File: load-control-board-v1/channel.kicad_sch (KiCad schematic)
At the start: 30 parts, among them Q2 IRFP7530PBF, U10 OPA188xxDBV, U11 INA186A1IDCKR, U9 OPA188xxDBV

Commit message: lc2kicad
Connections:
- net I_sink_mon_0 renamed I_sink_mon
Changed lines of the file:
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@@
 	)
 	(label "V_Rs0n"
-		(at 208.28 54.61 0)
+		(at 168.91 68.58 0)
 		(effects
 			(font
@@
 	)
 	(label "V_Rs0n"
-		(at 168.91 68.58 0)
+		(at 208.28 54.61 0)
 		(effects
 			(font
@@
 			)
 			(justify left bottom)
-		)
-	)
-	(global_label "I_sink_mon_0"
-		(shape input)
-		(at 248.92 69.85 0)
-		(fields_autoplaced yes)
-		(effects
-			(font
-				(size 1.27 1.27)
-			)
-			(justify left)
-		)
-		(property "Intersheetrefs" "${INTERSHEET_REFS}"
-			(at 264.4236 69.85 0)
-			(effects
-				(font
-					(size 1.27 1.27)
-				)
-				(justify left)
-				(hide yes)
-			)
 		)
 	)
@@
 		)
 	)
+	(hierarchical_label "I_sink_mon"
+		(shape input)
+		(at 248.92 69.85 0)
+		(effects
+			(font
+				(size 1.27 1.27)
+			)
+			(justify left)
+		)
+	)

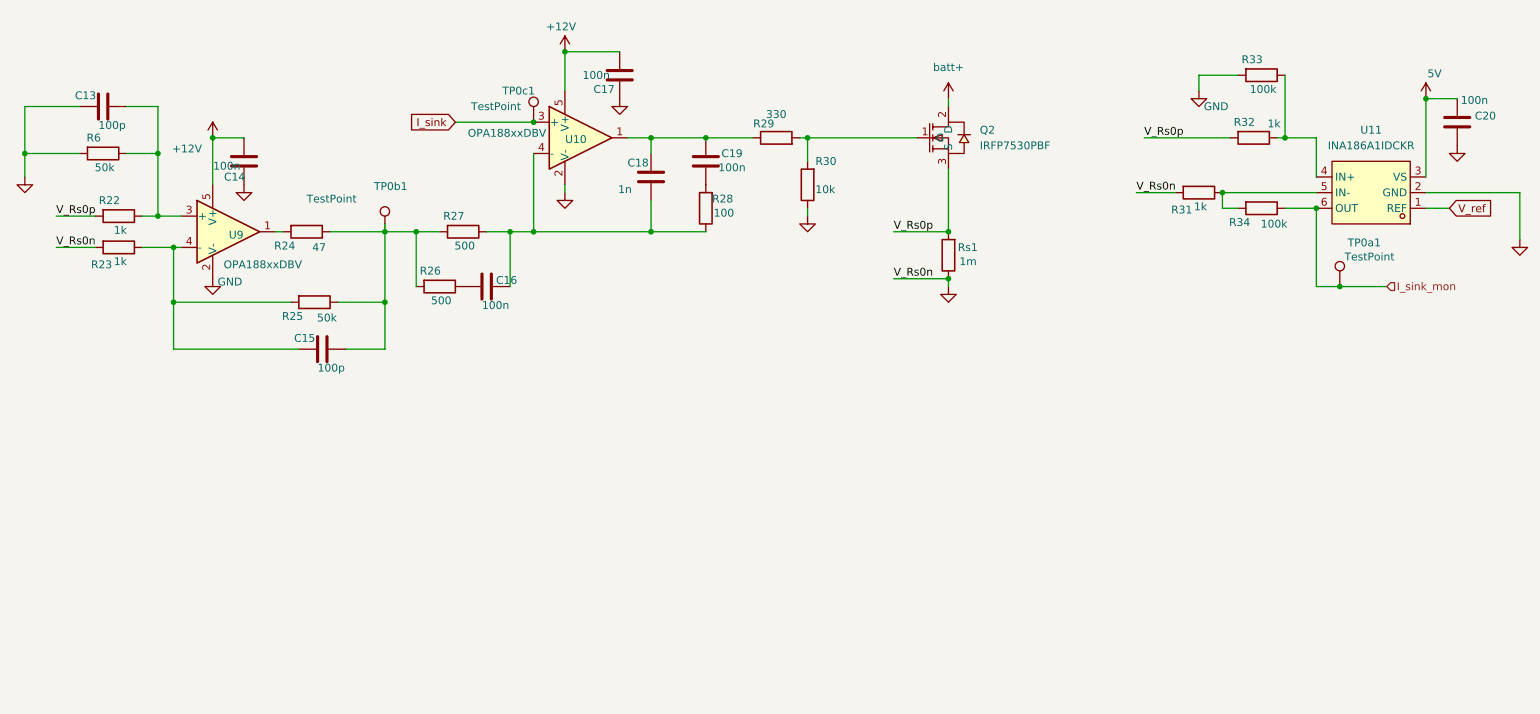
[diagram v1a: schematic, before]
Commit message: Edit multi opamp
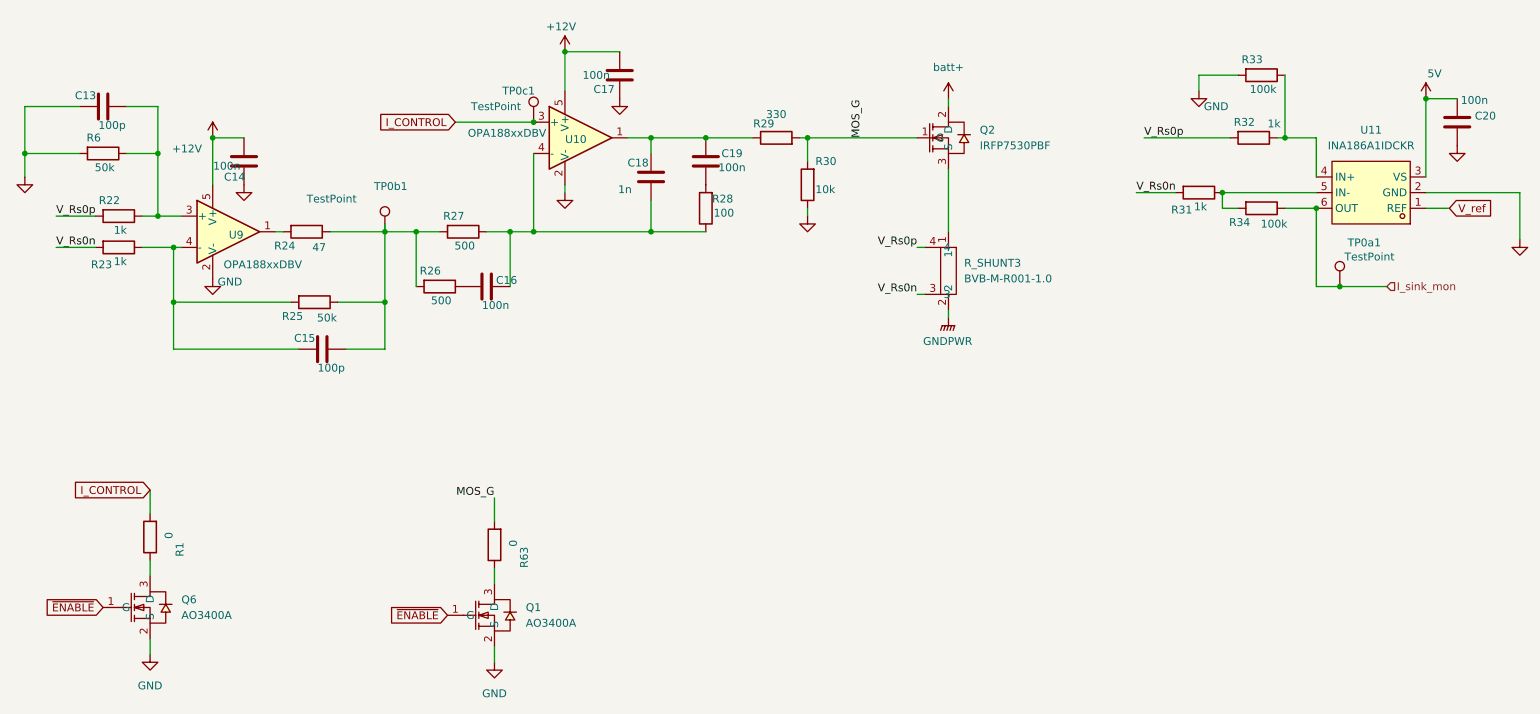
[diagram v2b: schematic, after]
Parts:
- removed Rs1: 1m, symbol Device:R
- added Q1, Q6: AO3400A, programmable-load-library:SOT-23-3_L2.9-W1.3-P1.90-LS2.4-BR, symbol programmable-load-library:AO3400A
- added R1, R63: 0, Resistor_SMD:R_0603_1608Metric, symbol Device:R
- added R_SHUNT3: BVB-M-R001-1.0, programmable-load-library:RES-SMD_4P-L6.9-W6.6_SBB-K-2F-N-T5, symbol programmable-load-library:BVB-M-R001-1.0
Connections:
- net GND: now also Q1.2 (S), Q6.2 (S); no longer R23.2, R31.2
- net V_Rs0p: now also R_SHUNT3.4; no longer Q2.3 (S)
- net MOS_G: now reaches Q2.1 (G), R29.2, R30.2
- net MOS_G: now also R63.2
- net I_sink renamed I_CONTROL
- net I_CONTROL: now also R1.2
- new net: Q1.3 (D), R63.1
- new net: Q2.3 (S), R_SHUNT3.1
- new net: Q6.3 (D), R1.1
- new net GNDPWR: R_SHUNT3.2
- new net V_Rs0n: R23.2, R31.2, R_SHUNT3.3
- new net ~{ENABLE}: Q1.1 (G), Q6.1 (G)

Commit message: Rearrange design in load control board, need further check
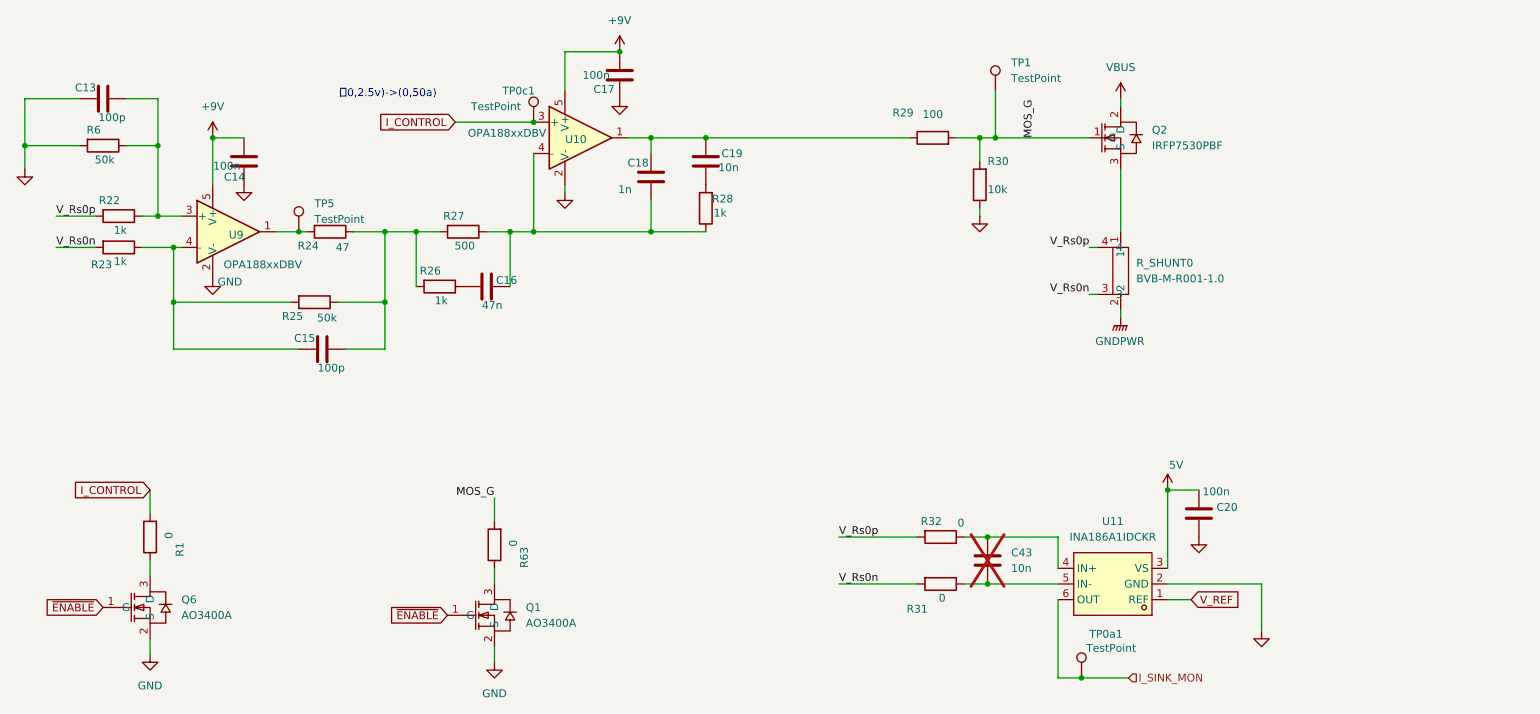
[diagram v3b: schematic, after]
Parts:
- removed R33, R34: 100k, Resistor_SMD:R_0603_1608Metric, symbol Device:R
- removed TP0b1: TestPoint, symbol Connector:TestPoint
- added C43: 10n, symbol Device:C
- added TP1, TP5: TestPoint, symbol Connector:TestPoint
- C16: value 100n -> 47n
- C19: value 100n -> 10n
- R26: value 500 -> 1k
- R28: value 100 -> 1k
- R29: value 330 -> 100
- R31, R32: value 1k -> 0
- renumbered R_SHUNT3 to R_SHUNT0
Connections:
- net MOS_G: now also TP1.1
- net at R24.2, U9.1: now also TP5.1
- net at R31.1, U11.5 (IN-): now also C43.2
- net at R32.1, U11.4 (IN+): now also C43.1
- net +12V renamed +9V
- net I_sink_mon renamed I_SINK_MON
- net V_ref renamed V_REF
- net batt+ renamed VBUS
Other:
- note added: "（0,2.5v)->(0,50a)"
- moved on the sheet: C13, C20, Q2, R24, R29, R30, R31, R32, R6, R_SHUNT0, TP0a1, U11
